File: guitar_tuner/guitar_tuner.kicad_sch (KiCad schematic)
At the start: 8 parts, among them SW1 Reset, SW2 Boot, U1 ESP32-S2-SOLO

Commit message: Quick Edits on Screen Connections
Quick Update
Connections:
- net GND: no longer U1.28 (SPIIO6/GPIO35/FSPID), U1.29 (SPIIO7/GPIO36/FSPICLK)
- new net Display/CS1: U1.28 (SPIIO6/GPIO35/FSPID)
- new net Display/SI: U1.29 (SPIIO7/GPIO36/FSPICLK)
- no-connect marks 23 -> 24
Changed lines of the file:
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@@
-	)
-	(junction
-		(at 55.88 95.25)
-		(diameter 0)
-		(color 0 0 0 0)
-	)
-	(junction
-		(at 55.88 92.71)
-		(diameter 0)
-		(color 0 0 0 0)
 	)
 	(junction
@@
 	)
 	(junction
-		(at 80.01 63.5)
+		(at 80.01 66.04)
 		(diameter 0)
 		(color 0 0 0 0)
@@
 	)
 	(junction
-		(at 55.88 87.63)
-		(diameter 0)
-		(color 0 0 0 0)
-	)
-	(junction
 		(at 204.47 73.66)
 		(diameter 0)
@@
 	)
 	(no_connect
+		(at 182.88 102.87)
+	)
+	(no_connect
 		(at 91.44 87.63)
 	)
@@
 	(wire
 		(pts
+			(xy 80.01 66.04) (xy 76.2 66.04)
+		)
+		(stroke
+			(width 0)
+			(type default)
+		)
+	)
+	(wire
+		(pts
 			(xy 74.93 74.93) (xy 76.2 74.93)
 		)
@@
 	(wire
 		(pts
-			(xy 55.88 66.04) (xy 66.04 66.04)
+			(xy 62.23 66.04) (xy 66.04 66.04)
 		)
 		(stroke
@@
 	(wire
 		(pts
-			(xy 72.39 95.25) (xy 72.39 149.86)
+			(xy 72.39 87.63) (xy 72.39 149.86)
 		)
 		(stroke
@@
 	(wire
 		(pts
-			(xy 87.63 63.5) (xy 87.63 62.23)
+			(xy 87.63 67.31) (xy 87.63 62.23)
 		)
 		(stroke
@@
 	(wire
 		(pts
-			(xy 80.01 62.23) (xy 80.01 63.5)
-		)
-		(stroke
-			(width 0)
-			(type default)
-		)
-	)
-	(wire
-		(pts
 			(xy 55.88 100.33) (xy 69.85 100.33)
 		)
@@
 	(wire
 		(pts
+			(xy 62.23 66.04) (xy 62.23 95.25)
+		)
+		(stroke
+			(width 0)
+			(type default)
+		)
+	)
+	(wire
+		(pts
 			(xy 69.85 152.4) (xy 194.31 152.4)
 		)
@@
 	(wire
 		(pts
-			(xy 55.88 66.04) (xy 55.88 87.63)
-		)
-		(stroke
-			(width 0)
-			(type default)
-		)
-	)
-	(wire
-		(pts
 			(xy 55.88 134.62) (xy 54.61 134.62)
 		)
@@
 	(wire
 		(pts
+			(xy 55.88 87.63) (xy 72.39 87.63)
+		)
+		(stroke
+			(width 0)
+			(type default)
+		)
+	)
+	(wire
+		(pts
 			(xy 87.63 62.23) (xy 91.44 62.23)
 		)
@@
 	(wire
 		(pts
-			(xy 55.88 95.25) (xy 72.39 95.25)
-		)
-		(stroke
-			(width 0)
-			(type default)
-		)
-	)
-	(wire
-		(pts
 			(xy 137.16 53.34) (xy 137.16 57.15)
 		)
@@
 	(wire
 		(pts
+			(xy 55.88 90.17) (xy 77.47 90.17)
+		)
+		(stroke
+			(width 0)
+			(type default)
+		)
+	)
+	(wire
+		(pts
 			(xy 137.16 50.8) (xy 137.16 53.34)
 		)
@@
 	(wire
 		(pts
+			(xy 82.55 67.31) (xy 82.55 66.04)
+		)
+		(stroke
+			(width 0)
+			(type default)
+		)
+	)
+	(wire
+		(pts
 			(xy 182.88 82.55) (xy 223.52 82.55)
 		)
@@
 	(wire
 		(pts
-			(xy 55.88 95.25) (xy 55.88 92.71)
-		)
-		(stroke
-			(width 0)
-			(type default)
-		)
-	)
-	(wire
-		(pts
 			(xy 72.39 149.86) (xy 193.04 149.86)
 		)
@@
 	(wire
 		(pts
-			(xy 55.88 87.63) (xy 55.88 92.71)
+			(xy 82.55 66.04) (xy 80.01 66.04)
+		)
+		(stroke
+			(width 0)
+			(type default)
+		)
+	)
+	(wire
+		(pts
+			(xy 62.23 95.25) (xy 55.88 95.25)
 		)
 		(stroke
@@
 	(wire
 		(pts
-			(xy 80.01 66.04) (xy 76.2 66.04)
-		)
-		(stroke
-			(width 0)
-			(type default)
-		)
-	)
-	(wire
-		(pts
 			(xy 219.71 110.49) (xy 182.88 110.49)
 		)
@@
 	(wire
 		(pts
-			(xy 80.01 63.5) (xy 87.63 63.5)
+			(xy 82.55 67.31) (xy 87.63 67.31)
 		)
 		(stroke
@@
 					(unit 1)
 				)
+			)
+		)
+	)
+	(symbol
+		(lib_name "+3.3V_1")
+		(lib_id "power:+3.3V")
+		(at 77.47 90.17 0)
+		(unit 1)
+		(exclude_from_sim no)
+		(in_bom yes)
+		(on_board yes)
+		(dnp no)
+		(fields_autoplaced yes)
+		(property "Reference" "#PWR033"
+			(at 77.47 93.98 0)
+			(effects
+				(font
+					(size 1.27 1.27)
+				)
+				(hide yes)
+			)
+		)
+		(property "Value" "+3.3V"
+			(at 77.47 85.09 0)
+			(effects
+				(font
+					(size 1.27 1.27)
+				)
+			)
+		)
+		(property "Footprint" ""
+			(at 77.47 90.17 0)
+			(effects
+				(font
+					(size 1.27 1.27)
+				)
+				(hide yes)
+			)
+		)
+		(property "Datasheet" ""
+			(at 77.47 90.17 0)
+			(effects
+				(font
+					(size 1.27 1.27)
+				)
+				(hide yes)
+			)
+		)
+		(property "Description" "Power symbol creates a global label with name \"+3.3V\""
+			(at 77.47 90.17 0)
+			(effects
+				(font
+					(size 1.27 1.27)
+				)
+				(hide yes)
+			)
+		)
+		(pin "1"
+		)
+		(instances
+			(project ""
+				(path "/66cd80e7-aa2b-4408-b572-7f7169004942"
+					(reference "#PWR033")
+					(unit 1)
+				)

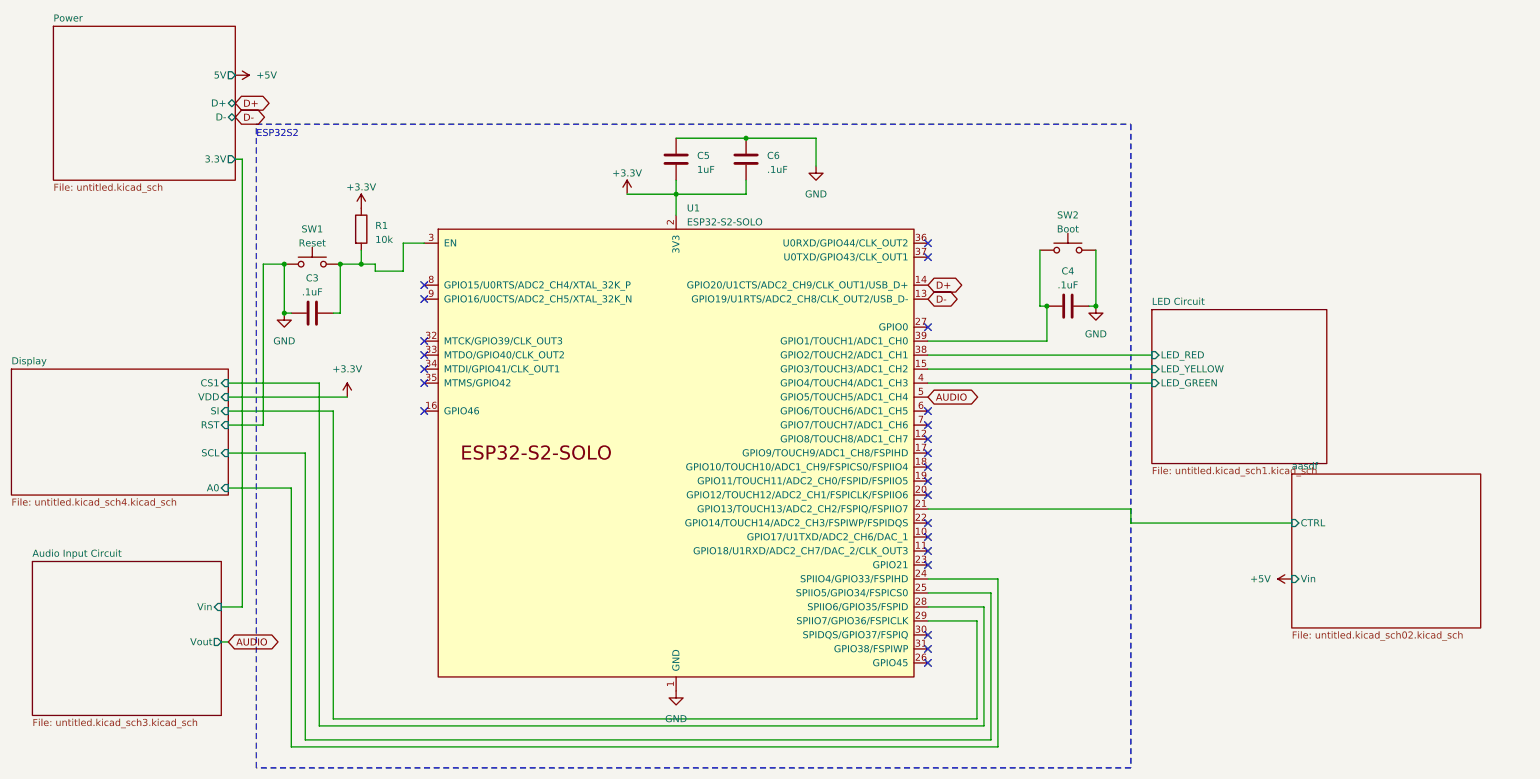
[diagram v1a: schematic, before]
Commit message: Edited names of subsheets
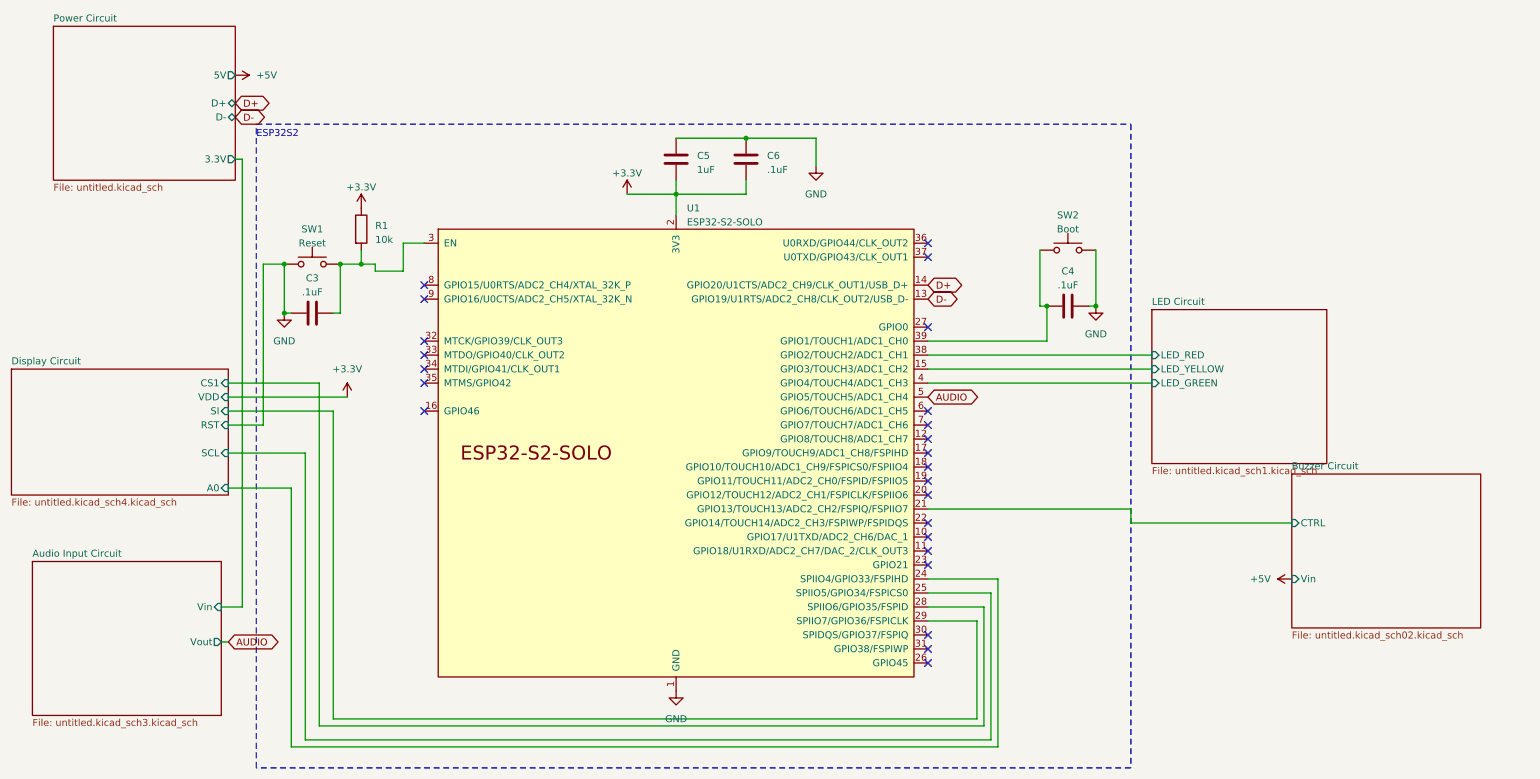
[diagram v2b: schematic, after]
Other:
- sheet Display renamed Display Circuit
- sheet Power renamed Power Circuit
- sheet aasdf renamed Buzzer Circuit
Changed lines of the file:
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@@
 			(color 0 0 0 0.0000)
 		)
-		(property "Sheetname" "Display"
+		(property "Sheetname" "Display Circuit"
 			(at 16.51 84.3784 0)
 			(effects
@@
 			(color 0 0 0 0.0000)
 		)
-		(property "Sheetname" "Power"
+		(property "Sheetname" "Power Circuit"
 			(at 24.13 22.1484 0)
 			(effects
@@
 			(color 0 0 0 0.0000)
 		)
-		(property "Sheetname" "aasdf"
+		(property "Sheetname" "Buzzer Circuit"
 			(at 248.92 103.4284 0)
 			(effects

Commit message: FootprintUpdate
Upodate to Footprints
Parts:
- C3, C4, C5, C6: footprint (none) -> Capacitor_SMD:C_0805_2012Metric_Pad1.18x1.45mm_HandSolder
- R1: footprint (none) -> Resistor_SMD:R_0805_2012Metric_Pad1.20x1.40mm_HandSolder
- SW1, SW2: footprint (none) -> Button_Switch_SMD:SW_Tactile_SPST_NO_Straight_CK_PTS636Sx25SMTRLFS
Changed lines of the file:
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@@
 			)
 		)
-		(property "Footprint" ""
+		(property "Footprint" "Capacitor_SMD:C_0805_2012Metric_Pad1.18x1.45mm_HandSolder"
 			(at 138.1252 50.8 0)
 			(effects
@@
 			)
 		)
-		(property "Footprint" ""
+		(property "Footprint" "Button_Switch_SMD:SW_Tactile_SPST_NO_Straight_CK_PTS636Sx25SMTRLFS"
 			(at 208.28 58.42 0)
 			(effects
@@
 			)
 		)
-		(property "Footprint" ""
+		(property "Footprint" "Capacitor_SMD:C_0805_2012Metric_Pad1.18x1.45mm_HandSolder"
 			(at 212.09 72.6948 0)
 			(effects
@@
 			)
 		)
-		(property "Footprint" ""
+		(property "Footprint" "Capacitor_SMD:C_0805_2012Metric_Pad1.18x1.45mm_HandSolder"
 			(at 74.93 73.9648 0)
 			(effects
@@
 			)
 		)
-		(property "Footprint" ""
+		(property "Footprint" "Resistor_SMD:R_0805_2012Metric_Pad1.20x1.40mm_HandSolder"
 			(at 78.232 59.69 90)
 			(effects
@@
 			)
 		)
-		(property "Footprint" ""
+		(property "Footprint" "Capacitor_SMD:C_0805_2012Metric_Pad1.18x1.45mm_HandSolder"
 			(at 150.8252 50.8 0)
 			(effects
@@
 			)
 		)
-		(property "Footprint" ""
+		(property "Footprint" "Button_Switch_SMD:SW_Tactile_SPST_NO_Straight_CK_PTS636Sx25SMTRLFS"
 			(at 71.12 60.96 0)
 			(effects

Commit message: ERC Complete
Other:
- sheet Display Circuit ports: added 3.3V; removed none
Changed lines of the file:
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@@
+	)
+	(junction
+		(at 77.47 90.17)
+		(diameter 0)
+		(color 0 0 0 0)
 	)
 	(junction
@@
 	)
 	(junction
+		(at 128.27 53.34)
+		(diameter 0)
+		(color 0 0 0 0)
+	)
+	(junction
 		(at 204.47 73.66)
 		(diameter 0)
@@
 	(wire
 		(pts
+			(xy 77.47 90.17) (xy 77.47 97.79)
+		)
+		(stroke
+			(width 0)
+			(type default)
+		)
+	)
+	(wire
+		(pts
 			(xy 58.42 128.27) (xy 54.61 128.27)
 		)
@@
 	(wire
 		(pts
+			(xy 86.36 53.34) (xy 128.27 53.34)
+		)
+		(stroke
+			(width 0)
+			(type default)
+		)
+	)
+	(wire
+		(pts
 			(xy 204.47 73.66) (xy 203.2 73.66)
 		)
@@
 	(wire
 		(pts
+			(xy 86.36 90.17) (xy 86.36 53.34)
+		)
+		(stroke
+			(width 0)
+			(type default)
+		)
+	)
+	(wire
+		(pts
 			(xy 66.04 74.93) (xy 66.04 66.04)
 		)
@@
 	(wire
 		(pts
+			(xy 77.47 90.17) (xy 86.36 90.17)
+		)
+		(stroke
+			(width 0)
+			(type default)
+		)
+	)
+	(wire
+		(pts
 			(xy 74.93 92.71) (xy 74.93 148.59)
 		)
@@
 		(pts
 			(xy 219.71 110.49) (xy 182.88 110.49)
+		)
+		(stroke
+			(width 0)
+			(type default)
+		)
+	)
+	(wire
+		(pts
+			(xy 77.47 97.79) (xy 55.88 97.79)
 		)
 		(stroke
@@
 				(path "/66cd80e7-aa2b-4408-b572-7f7169004942"
 					(reference "#PWR010")
-					(unit 1)
-				)
-			)
-		)
-	)
-	(symbol
-		(lib_name "+3.3V_1")
-		(lib_id "power:+3.3V")
-		(at 77.47 90.17 0)
-		(unit 1)
-		(exclude_from_sim no)
-		(in_bom yes)
-		(on_board yes)
-		(dnp no)
-		(fields_autoplaced yes)
-		(property "Reference" "#PWR033"
-			(at 77.47 93.98 0)
-			(effects
-				(font
-					(size 1.27 1.27)
-				)
-				(hide yes)
-			)
-		)
-		(property "Value" "+3.3V"
-			(at 77.47 85.09 0)
-			(effects
-				(font
-					(size 1.27 1.27)
-				)
-			)
-		)
-		(property "Footprint" ""
-			(at 77.47 90.17 0)
-			(effects
-				(font
-					(size 1.27 1.27)
-				)
-				(hide yes)
-			)
-		)
-		(property "Datasheet" ""
-			(at 77.47 90.17 0)
-			(effects
-				(font
-					(size 1.27 1.27)
-				)
-				(hide yes)
-			)
-		)
-		(property "Description" "Power symbol creates a global label with name \"+3.3V\""
-			(at 77.47 90.17 0)
-			(effects
-				(font
-					(size 1.27 1.27)
-				)
-				(hide yes)
-			)
-		)
-		(pin "1"
-		)
-		(instances
-			(project ""
-				(path "/66cd80e7-aa2b-4408-b572-7f7169004942"
-					(reference "#PWR033")
 					(unit 1)
 				)
@@
 			(effects
 				(font
+					(size 1.27 1.27)
+				)
+				(justify right)
+			)
+		)
+		(pin "3.3V" input
+			(at 55.88 97.79 0)
+			(effects
+				(font

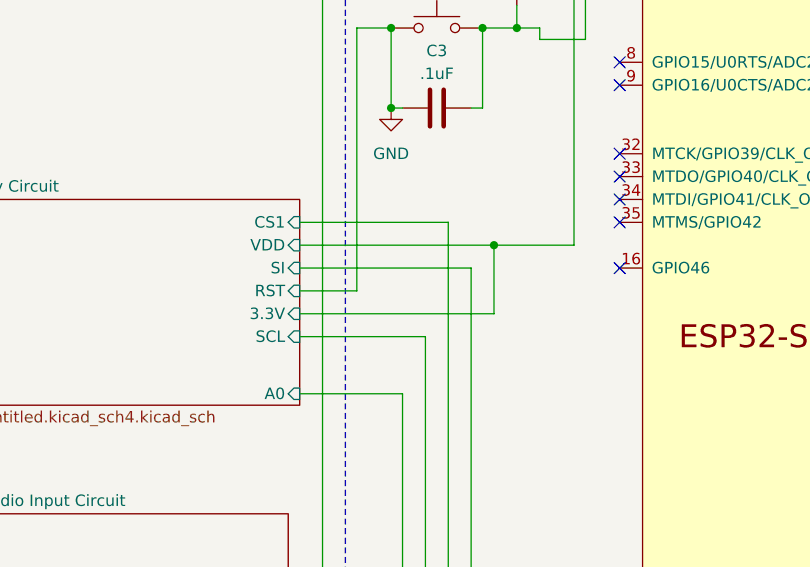
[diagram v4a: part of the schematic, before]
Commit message: ERC Check
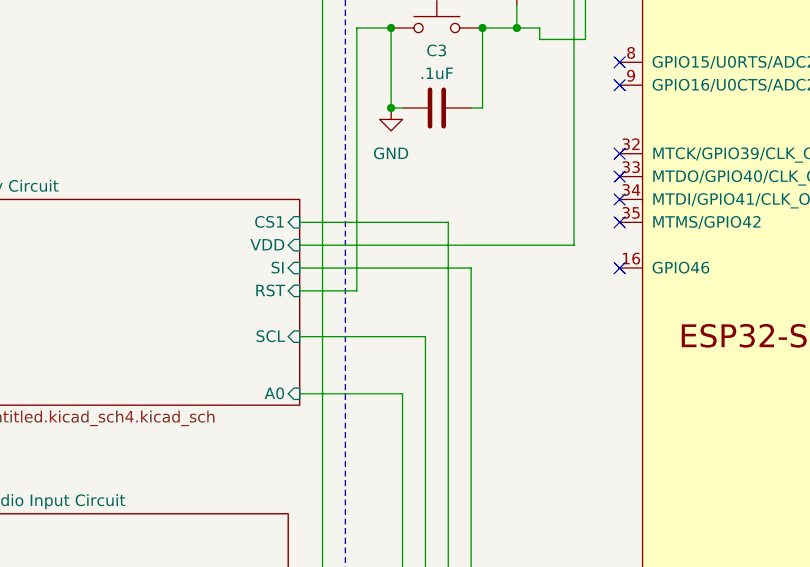
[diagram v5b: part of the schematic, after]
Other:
- sheet Display Circuit ports: added none; removed 3.3V
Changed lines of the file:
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@@
-	)
-	(junction
-		(at 77.47 90.17)
-		(diameter 0)
-		(color 0 0 0 0)
 	)
 	(junction
@@
 	(wire
 		(pts
-			(xy 77.47 90.17) (xy 77.47 97.79)
-		)
-		(stroke
-			(width 0)
-			(type default)
-		)
-	)
-	(wire
-		(pts
 			(xy 58.42 128.27) (xy 54.61 128.27)
 		)
@@
 	(wire
 		(pts
-			(xy 77.47 90.17) (xy 86.36 90.17)
+			(xy 55.88 90.17) (xy 86.36 90.17)
 		)
 		(stroke
@@
 	(wire
 		(pts
-			(xy 55.88 90.17) (xy 77.47 90.17)
-		)
-		(stroke
-			(width 0)
-			(type default)
-		)
-	)
-	(wire
-		(pts
 			(xy 137.16 50.8) (xy 137.16 53.34)
 		)
@@
 		(pts
 			(xy 219.71 110.49) (xy 182.88 110.49)
-		)
-		(stroke
-			(width 0)
-			(type default)
-		)
-	)
-	(wire
-		(pts
-			(xy 77.47 97.79) (xy 55.88 97.79)
 		)
 		(stroke
@@
 			(effects
 				(font
-					(size 1.27 1.27)
-				)
-				(justify right)
-			)
-		)
-		(pin "3.3V" input
-			(at 55.88 97.79 0)
-			(effects
-				(font

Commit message: Footprint Fix
I hope
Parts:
- U1: footprint PCM_Espressif:ESP32-S2-SOLO -> Library:MOD41_ESP32-S2-SOLO_EXP
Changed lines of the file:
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@@
 			)
 		)
-		(property "Footprint" "PCM_Espressif:ESP32-S2-SOLO"
+		(property "Footprint" "Library:MOD41_ESP32-S2-SOLO_EXP"
 			(at 137.16 153.67 0)
 			(effects
